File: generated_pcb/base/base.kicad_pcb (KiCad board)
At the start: 2 copper layers, 114.5 x 101.2 mm, 0 parts

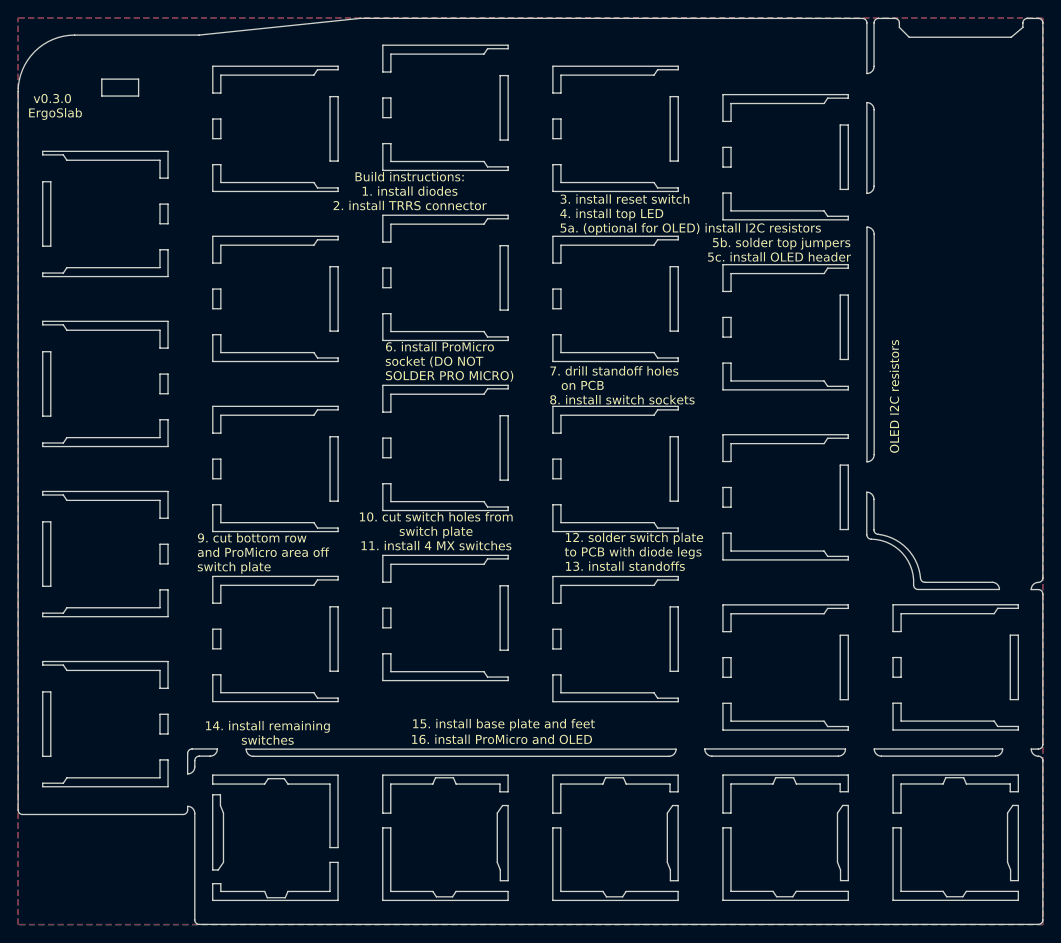
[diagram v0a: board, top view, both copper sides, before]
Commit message: fix: make sure edge.cuts remain on base layer, figure out how to read line width in python script
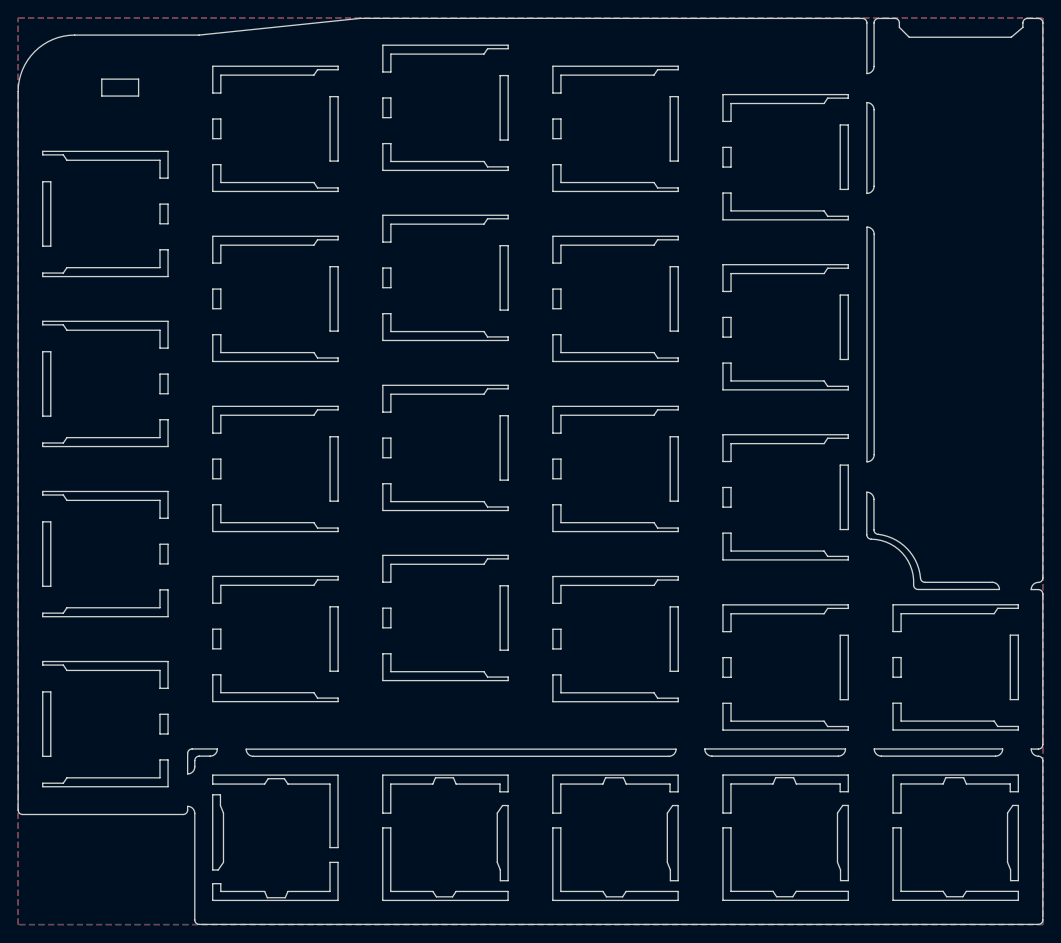
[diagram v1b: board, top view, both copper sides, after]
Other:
- board text removed: "10. cut switch holes from switch plate 11. install 4 MX switches"
- board text removed: "12. solder switch plate to PCB with diode legs 13. install standoffs"
- board text removed: "14. install remaining switches"
- board text removed: "15. install base plate and feet"
- board text removed: "16. install ProMicro and OLED"
- board text removed: "3. install reset switch 4. install top LED 5a. (optional for OLED) install I2C resistors"
- board text removed: "5b. solder top jumpers 5c. install OLED header"
- board text removed: "6. install ProMicro socket (DO NOT SOLDER PRO MICRO)"
- board text removed: "7. drill standoff holes on PCB 8. install switch sockets"
- board text removed: "9. cut bottom row and ProMicro area off switch plate"
- board text removed: "Build instructions: 1. install diodes 2. install TRRS connector"
- board text removed: "Designed by Tom Saleeba. Copyright 2019 - MIT License"
- board text removed: "ErgoSlab"
- board text removed: "OLED I2C resistors"
- board text removed: "v0.3.0"
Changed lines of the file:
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@@
   (general
     (thickness 1.6)
-    (drawings 751)
+    (drawings 734)
     (tracks 0)
     (zones 0)
@@
   (gr_line (start 156.795 129.74) (end 152.095 129.74) (layer Edge.Cuts) (width 0.05))
   (gr_line (start 152.095 141.74) (end 156.795 141.74) (layer Edge.Cuts) (width 0.05))
-  (gr_text "15. install base plate and feet" (at 126.68 123.05) (layer F.SilkS)
-    (effects (font (size 1 1) (thickness 0.15)))
-  )
-  (gr_text "OLED I2C resistors" (at 170.4 86.45 90) (layer F.SilkS)
-    (effects (font (size 1 1) (thickness 0.15)))
-  )
-  (gr_text "16. install ProMicro and OLED" (at 126.48 124.8) (layer F.SilkS)
-    (effects (font (size 1 1) (thickness 0.15)))
-  )
-  (gr_text "10. cut switch holes from\nswitch plate\n11. install 4 MX switches" (at 119.15 101.55) (layer F.SilkS)
-    (effects (font (size 1 1) (thickness 0.15)))
-  )
-  (gr_text "14. install remaining\nswitches" (at 100.34 124.08) (layer F.SilkS)
-    (effects (font (size 1 1) (thickness 0.15)))
-  )
-  (gr_text "12. solder switch plate\nto PCB with diode legs\n13. install standoffs" (at 133.5 103.85) (layer F.SilkS)
-    (effects (font (size 1 1) (thickness 0.15)) (justify left))
-  )
-  (gr_text "9. cut bottom row\nand ProMicro area off\nswitch plate" (at 92.45 103.9) (layer F.SilkS)
-    (effects (font (size 1 1) (thickness 0.15)) (justify left))
-  )
-  (gr_text "7. drill standoff holes\n   on PCB\n8. install switch sockets" (at 131.8 85.25) (layer F.SilkS)
-    (effects (font (size 1 1) (thickness 0.15)) (justify left))
-  )
-  (gr_text "6. install ProMicro\nsocket (DO NOT \nSOLDER PRO MICRO)" (at 113.45 82.55) (layer F.SilkS)
-    (effects (font (size 1 1) (thickness 0.15)) (justify left))
-  )
-  (gr_text "5b. solder top jumpers\n5c. install OLED header" (at 165.5 70.1) (layer F.SilkS)
-    (effects (font (size 1 1) (thickness 0.15)) (justify right))
-  )
-  (gr_text "3. install reset switch\n4. install top LED\n5a. (optional for OLED) install I2C resistors" (at 132.95 66.05) (layer F.SilkS)
-    (effects (font (size 1 1) (thickness 0.15)) (justify left))
-  )
-  (gr_text "Build instructions:\n1. install diodes\n2. install TRRS connector" (at 116.2 63.55) (layer F.SilkS)
-    (effects (font (size 1 1) (thickness 0.15)))
-  )
-  (gr_text "Designed by Tom Saleeba. Copyright 2019 - MIT License" (at 160.714286 143.85) (layer B.SilkS)
-    (effects (font (size 1 1) (thickness 0.15)) (justify left mirror))
-  )
-  (gr_text ErgoSlab (at 76.6 54.8) (layer F.SilkS)
-    (effects (font (size 1 1) (thickness 0.15)))
-  )
   (gr_line (start 167.28 53.61) (end 167.28 63.76) (layer Edge.Cuts) (width 0.05))
   (gr_line (start 168.08 54.41) (end 168.08 62.96) (layer Edge.Cuts) (width 0.05))
-  (gr_text v0.3.0 (at 76.3 53.2) (layer F.SilkS)
-    (effects (font (size 1 1) (thickness 0.15)))
-  )
   (gr_line (start 97.93 125.85) (end 145.96 125.85) (layer Edge.Cuts) (width 0.05))
   (gr_line (start 98.73 126.65) (end 145.16 126.65) (layer Edge.Cuts) (width 0.05))
@@
   (gr_line (start 183.41 46.31) (end 184.71 45.21) (layer Edge.Cuts) (width 0.05))
   (gr_line (start 172.01 46.31) (end 183.41 46.31) (layer Edge.Cuts) (width 0.05))
-  (dimension 101.37 (width 0.12) (layer Dwgs.User)
-    (gr_text "101.370 mm" (at 68.377306 94.745 90) (layer Dwgs.User)
-      (effects (font (size 1 1) (thickness 0.15)))
-    )
-    (feature1 (pts (xy 72.2 44.06) (xy 69.060885 44.06)))
-    (feature2 (pts (xy 72.2 145.43) (xy 69.060885 145.43)))
-    (crossbar (pts (xy 69.647306 145.43) (xy 69.647306 44.06)))
-    (arrow1a (pts (xy 69.647306 44.06) (xy 70.233727 45.186504)))
-    (arrow1b (pts (xy 69.647306 44.06) (xy 69.060885 45.186504)))
-    (arrow2a (pts (xy 69.647306 145.43) (xy 70.233727 144.303496)))
-    (arrow2b (pts (xy 69.647306 145.43) (xy 69.060885 144.303496)))
-  )
-  (dimension 114.56 (width 0.12) (layer Dwgs.User)
-    (gr_text "114.560 mm" (at 129.63 41.44) (layer Dwgs.User)
-      (effects (font (size 1 1) (thickness 0.15)))
-    )
-    (feature1 (pts (xy 186.91 45.86) (xy 186.91 42.123579)))
-    (feature2 (pts (xy 72.35 45.86) (xy 72.35 42.123579)))
-    (crossbar (pts (xy 72.35 42.71) (xy 186.91 42.71)))
-    (arrow1a (pts (xy 186.91 42.71) (xy 185.783496 43.296421)))
-    (arrow1b (pts (xy 186.91 42.71) (xy 185.783496 42.123579)))
-    (arrow2a (pts (xy 72.35 42.71) (xy 73.476504 43.296421)))
-    (arrow2b (pts (xy 72.35 42.71) (xy 73.476504 42.123579)))
-  )
   (zone (net 0) (net_name "") (layer B.Cu) (hatch edge 0.508)
     (connect_pads (clearance 0.508))

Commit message: fix: generating something for all layers, outline is good, zones are refilled, still more to do
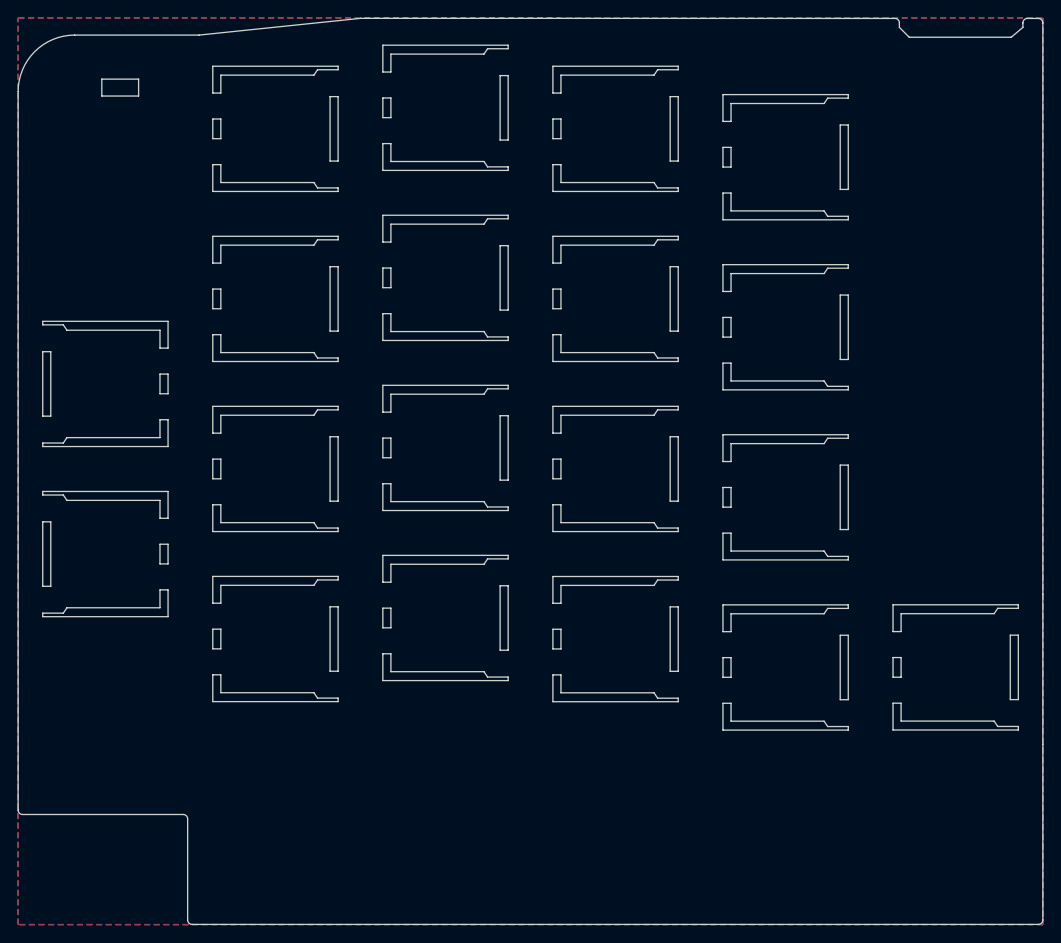
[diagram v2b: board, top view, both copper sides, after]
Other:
- outline, holes or cut-outs redrawn

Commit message: feat: completed the new approach of generating PCBs from the master
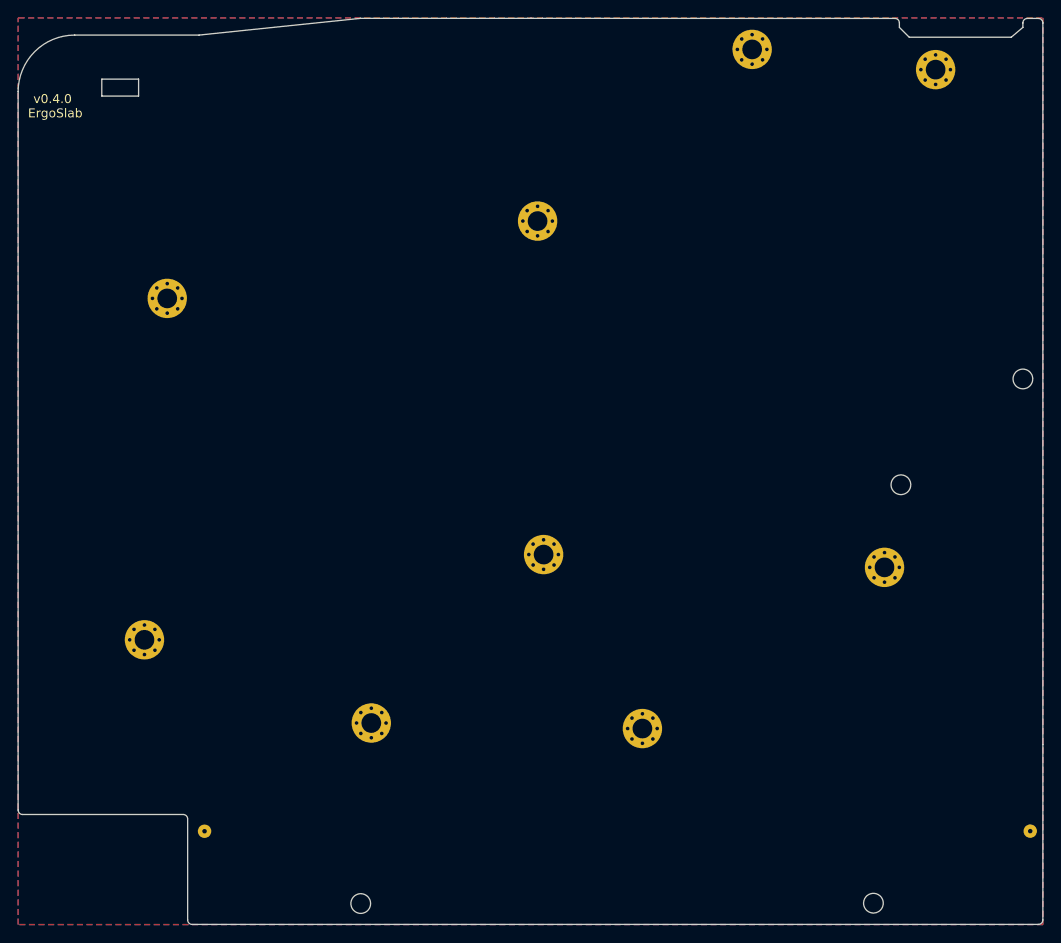
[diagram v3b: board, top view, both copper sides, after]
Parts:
- added BraceNotTop0: switchplate-brace, footprints:switchplate-brace, F.Cu at (93.3, 135.0)
- added BraceNotTop1: switchplate-brace, footprints:switchplate-brace, F.Cu at (185.5, 135.0)
- added CHICKEN: LOGO, footprints:chicken, B.Cu at (177.9, 67.5)
- added Mount0: MountingHole_2.2mm_M2_Pad_Via, MountingHole:MountingHole_2.2mm_M2_Pad_Via, F.Cu at (154.5, 47.7)
- added Mount1: MountingHole_2.2mm_M2_Pad_Via, MountingHole:MountingHole_2.2mm_M2_Pad_Via, F.Cu at (89.1, 75.5)
- added Mount2: MountingHole_2.2mm_M2_Pad_Via, MountingHole:MountingHole_2.2mm_M2_Pad_Via, F.Cu at (130.5, 66.8)
- added Mount3: MountingHole_2.2mm_M2_Pad_Via, MountingHole:MountingHole_2.2mm_M2_Pad_Via, F.Cu at (86.6, 113.6)
- added Mount4: MountingHole_2.2mm_M2_Pad_Via, MountingHole:MountingHole_2.2mm_M2_Pad_Via, F.Cu at (131.2, 104.1)
- added Mount5: MountingHole_2.2mm_M2_Pad_Via, MountingHole:MountingHole_2.2mm_M2_Pad_Via, F.Cu at (169.2, 105.5)
- added Mount6: MountingHole_2.2mm_M2_Pad_Via, MountingHole:MountingHole_2.2mm_M2_Pad_Via, F.Cu at (111.9, 122.9)
- added Mount7: MountingHole_2.2mm_M2_Pad_Via, MountingHole:MountingHole_2.2mm_M2_Pad_Via, F.Cu at (142.2, 123.5)
- added MountNotTop0: MountingHole_2.2mm_M2_Pad_Via, MountingHole:MountingHole_2.2mm_M2_Pad_Via, F.Cu at (175.0, 49.9)
- added MountNotTop1: VAL**, footprints:HOLE_M2, F.Cu at (184.7, 84.5)
- added MountNotTop2: VAL**, footprints:HOLE_M2, F.Cu at (171.1, 96.3)
- added MountNotTop3: VAL**, footprints:HOLE_M2, F.Cu at (110.7, 143.1)
- added MountNotTop4: VAL**, footprints:HOLE_M2, F.Cu at (168.0, 143.1)
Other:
- outline, holes or cut-outs redrawn
- board text added: "ErgoSlab"
- board text added: "v0.4.0"

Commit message: chore: bump version to 1.0.0 now I know it works (typing on it right now), give OLED resistor more space, make choc row M2 mounts more obvious, fix up silk screen build instructions
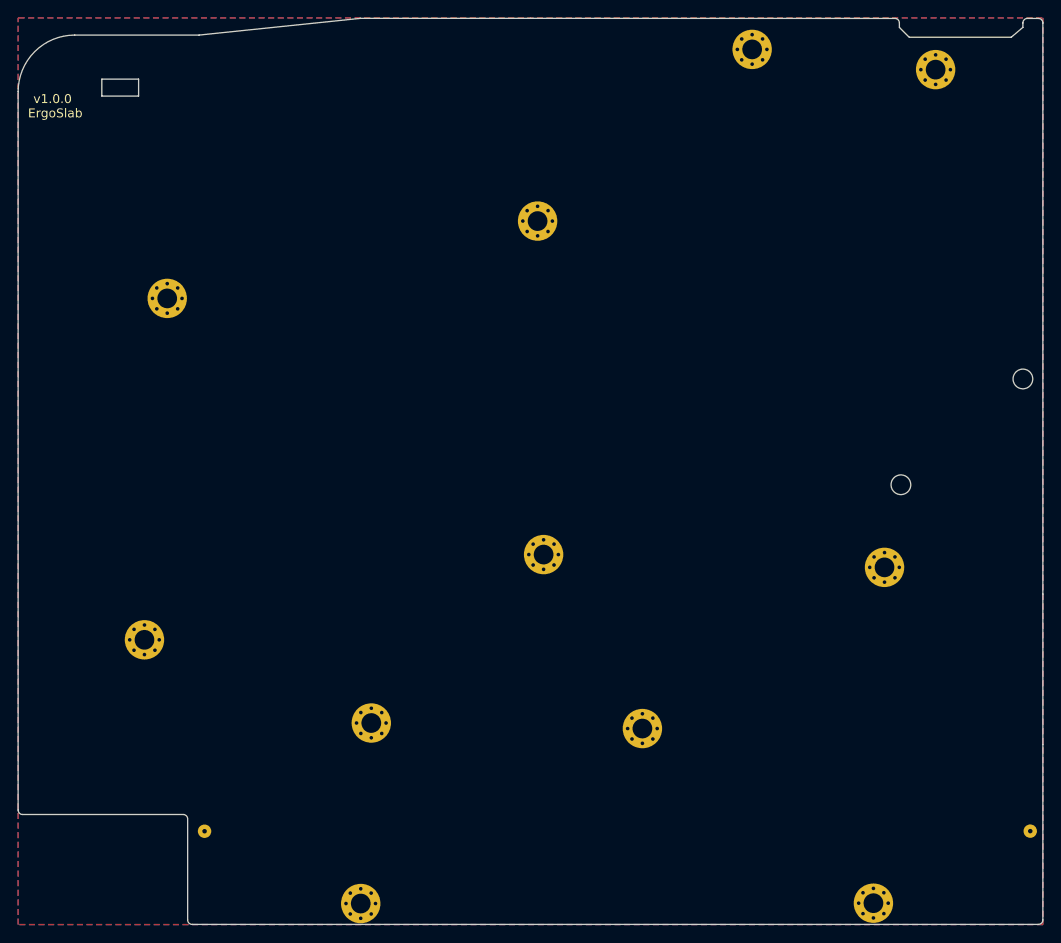
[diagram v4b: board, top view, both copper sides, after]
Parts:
- MountNotTop3, MountNotTop4: value VAL** -> MountingHole_2.2mm_M2_Pad_Via; footprint footprints:HOLE_M2 -> MountingHole:MountingHole_2.2mm_M2_Pad_Via
- turned MountNotTop3 to 270 degrees
- turned MountNotTop4 to 270 degrees
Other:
- board text added: "v1.0.0"
- board text removed: "v0.4.0"
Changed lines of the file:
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@@
   (title_block
     (title ErgoSlab)
-    (rev 0.4.0)
+    (rev 1.0.0)
     (company "By Tom Saleeba")
     (comment 1 "MIT License")
@@
     (uvia_dia 0.8)
     (uvia_drill 0.4)
+  )
+  (module MountingHole:MountingHole_2.2mm_M2_Pad_Via (layer F.Cu)
+    (at 168.01 143.06 270)
+    (descr "Mounting Hole 2.2mm, M2")
+    (tags "mounting hole 2.2mm m2")
+    (attr virtual)
+    (fp_text reference MountNotTop4 (at 0 -3.2 90) (layer F.SilkS) hide
+      (effects (font (size 1 1) (thickness 0.15)))
+    )
+    (fp_text value MountingHole_2.2mm_M2_Pad_Via (at 0 3.2 90) (layer F.Fab)
+      (effects (font (size 1 1) (thickness 0.15)))
+    )
+    (fp_circle (center 0 0) (end 2.45 0) (layer F.CrtYd) (width 0.05))
+    (fp_circle (center 0 0) (end 2.2 0) (layer Cmts.User) (width 0.15))
+    (fp_text user %R (at 0.3 0 90) (layer F.Fab)
+      (effects (font (size 1 1) (thickness 0.15)))
+    )
+    (pad 1 thru_hole circle (at 1.166726 -1.166726 270) (size 0.7 0.7) (drill 0.4) (layers *.Cu *.Mask))
+    (pad 1 thru_hole circle (at 0 -1.65 270) (size 0.7 0.7) (drill 0.4) (layers *.Cu *.Mask))
+    (pad 1 thru_hole circle (at -1.166726 -1.166726 270) (size 0.7 0.7) (drill 0.4) (layers *.Cu *.Mask))
+    (pad 1 thru_hole circle (at -1.65 0 270) (size 0.7 0.7) (drill 0.4) (layers *.Cu *.Mask))
+    (pad 1 thru_hole circle (at -1.166726 1.166726 270) (size 0.7 0.7) (drill 0.4) (layers *.Cu *.Mask))
+    (pad 1 thru_hole circle (at 0 1.65 270) (size 0.7 0.7) (drill 0.4) (layers *.Cu *.Mask))
+    (pad 1 thru_hole circle (at 1.166726 1.166726 270) (size 0.7 0.7) (drill 0.4) (layers *.Cu *.Mask))
+    (pad 1 thru_hole circle (at 1.65 0 270) (size 0.7 0.7) (drill 0.4) (layers *.Cu *.Mask))
+    (pad 1 thru_hole circle (at 0 0 270) (size 4.4 4.4) (drill 2.2) (layers *.Cu *.Mask))
+  )
+  (module MountingHole:MountingHole_2.2mm_M2_Pad_Via (layer F.Cu)
+    (at 110.73 143.1 270)
+    (descr "Mounting Hole 2.2mm, M2")
+    (tags "mounting hole 2.2mm m2")
+    (attr virtual)
+    (fp_text reference MountNotTop3 (at 0 -3.2 90) (layer F.SilkS) hide
+      (effects (font (size 1 1) (thickness 0.15)))
+    )
+    (fp_text value MountingHole_2.2mm_M2_Pad_Via (at 0 3.2 90) (layer F.Fab)
+      (effects (font (size 1 1) (thickness 0.15)))
+    )
+    (fp_text user %R (at 0.3 0 90) (layer F.Fab)
+      (effects (font (size 1 1) (thickness 0.15)))
+    )
+    (fp_circle (center 0 0) (end 2.2 0) (layer Cmts.User) (width 0.15))
+    (fp_circle (center 0 0) (end 2.45 0) (layer F.CrtYd) (width 0.05))
+    (pad 1 thru_hole circle (at 0 0 270) (size 4.4 4.4) (drill 2.2) (layers *.Cu *.Mask))
+    (pad 1 thru_hole circle (at 1.65 0 270) (size 0.7 0.7) (drill 0.4) (layers *.Cu *.Mask))
+    (pad 1 thru_hole circle (at 1.166726 1.166726 270) (size 0.7 0.7) (drill 0.4) (layers *.Cu *.Mask))
+    (pad 1 thru_hole circle (at 0 1.65 270) (size 0.7 0.7) (drill 0.4) (layers *.Cu *.Mask))
+    (pad 1 thru_hole circle (at -1.166726 1.166726 270) (size 0.7 0.7) (drill 0.4) (layers *.Cu *.Mask))
+    (pad 1 thru_hole circle (at -1.65 0 270) (size 0.7 0.7) (drill 0.4) (layers *.Cu *.Mask))
+    (pad 1 thru_hole circle (at -1.166726 -1.166726 270) (size 0.7 0.7) (drill 0.4) (layers *.Cu *.Mask))
+    (pad 1 thru_hole circle (at 0 -1.65 270) (size 0.7 0.7) (drill 0.4) (layers *.Cu *.Mask))
+    (pad 1 thru_hole circle (at 1.166726 -1.166726 270) (size 0.7 0.7) (drill 0.4) (layers *.Cu *.Mask))
   )
   (module footprints:chicken (layer B.Cu)
@@
       (clearance 0.85))
   )
-  (module footprints:HOLE_M2 (layer F.Cu)
-    (at 110.73 143.1)
-    (fp_text reference MountNotTop3 (at 0 -2) (layer F.SilkS) hide
-      (effects (font (size 0.29972 0.29972) (thickness 0.07493)))
-    )
-    (fp_text value VAL** (at 0 1.75) (layer F.SilkS) hide
-      (effects (font (size 0.29972 0.29972) (thickness 0.0762)))
-    )
-    (pad "" np_thru_hole circle (at 0 0) (size 2.2 2.2) (drill 2.2) (layers *.Cu *.Mask F.SilkS)
-      (clearance 0.85))
-  )
-  (module footprints:HOLE_M2 (layer F.Cu)
-    (at 168.01 143.06)
-    (fp_text reference MountNotTop4 (at 0 -2) (layer F.SilkS) hide
-      (effects (font (size 0.29972 0.29972) (thickness 0.07493)))
-    )
-    (fp_text value VAL** (at 0 1.75) (layer F.SilkS) hide
-      (effects (font (size 0.29972 0.29972) (thickness 0.0762)))
-    )
-    (pad "" np_thru_hole circle (at 0 0) (size 2.2 2.2) (drill 2.2) (layers *.Cu *.Mask F.SilkS)
-      (clearance 0.85))
-  )
   (module footprints:switchplate-brace (layer F.Cu)
     (at 185.53 135.01)
@@
     (effects (font (size 1 1) (thickness 0.1501)))
   )
-  (gr_text v0.4.0 (at 76.3 53.2) (layer F.SilkS)
+  (gr_text v1.0.0 (at 76.3 53.2) (layer F.SilkS)
     (effects (font (size 1 1) (thickness 0.1501)))
   )
